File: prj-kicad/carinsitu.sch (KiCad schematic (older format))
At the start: 0 parts

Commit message: = ADD: Draw board outline, add fix holes
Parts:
- added FIX1, FIX2, FIX3, FIX4, FIX5: CONN_1, carinsitu:FIX, symbol CONN_1
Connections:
- new net GND: FIX1.1, FIX2.1, FIX3.1, FIX4.1, FIX5.1
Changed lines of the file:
@@
 EESchema Schematic File Version 2
-LIBS:power
+LIBS:cartes_v3
+LIBS:carinsitu
 LIBS:carinsitu-cache
 EELAYER 25 0
@@
 Comment4 ""
 $EndDescr
+$Comp
+L CONN_1 FIX1
+U 1 1 5D08E86D
+P 6050 6800
+F 0 "FIX1" H 6130 6800 40  0000 L CNN
+F 1 "CONN_1" H 6050 6855 30  0001 C CNN
+F 2 "carinsitu:FIX" H 6050 6800 60  0001 C CNN
+F 3 "" H 6050 6800 60  0000 C CNN
+	1    6050 6800
+	-1   0    0    1
+$EndComp
+$Comp
+L CONN_1 FIX2
+U 1 1 5D08E8D7
+P 6050 6950
+F 0 "FIX2" H 6130 6950 40  0000 L CNN
+F 1 "CONN_1" H 6050 7005 30  0001 C CNN
+F 2 "carinsitu:FIX" H 6050 6950 60  0001 C CNN
+F 3 "" H 6050 6950 60  0000 C CNN
+	1    6050 6950
+	-1   0    0    1
+$EndComp
+$Comp
+L CONN_1 FIX3
+U 1 1 5D08E908
+P 6050 7100
+F 0 "FIX3" H 6130 7100 40  0000 L CNN
+F 1 "CONN_1" H 6050 7155 30  0001 C CNN
+F 2 "carinsitu:FIX" H 6050 7100 60  0001 C CNN
+F 3 "" H 6050 7100 60  0000 C CNN
+	1    6050 7100
+	-1   0    0    1
+$EndComp
+$Comp
+L CONN_1 FIX4
+U 1 1 5D08E927
+P 6050 7250
+F 0 "FIX4" H 6130 7250 40  0000 L CNN
+F 1 "CONN_1" H 6050 7305 30  0001 C CNN
+F 2 "carinsitu:FIX" H 6050 7250 60  0001 C CNN
+F 3 "" H 6050 7250 60  0000 C CNN
+	1    6050 7250
+	-1   0    0    1
+$EndComp
+$Comp
+L CONN_1 FIX5
+U 1 1 5D08E968
+P 6050 7400
+F 0 "FIX5" H 6130 7400 40  0000 L CNN
+F 1 "CONN_1" H 6050 7455 30  0001 C CNN
+F 2 "carinsitu:FIX" H 6050 7400 60  0001 C CNN
+F 3 "" H 6050 7400 60  0000 C CNN
+	1    6050 7400
+	-1   0    0    1
+$EndComp
+$Comp
+L GND #PWR01
+U 1 1 5D08EA24
+P 6300 7500
+F 0 "#PWR01" H 6300 7500 30  0001 C CNN
+F 1 "GND" H 6300 7430 30  0001 C CNN
+F 2 "" H 6300 7500 60  0000 C CNN
+F 3 "" H 6300 7500 60  0000 C CNN
+	1    6300 7500
+	1    0    0    -1
+$EndComp
+Wire Wire Line
+	6200 6800 6300 6800
+Wire Wire Line
+	6300 6800 6300 7500
+Wire Wire Line
+	6200 6950 6300 6950
+Connection ~ 6300 6950
+Wire Wire Line
+	6200 7100 6300 7100
+Connection ~ 6300 7100
+Wire Wire Line
+	6200 7250 6300 7250
+Connection ~ 6300 7250
+Wire Wire Line
+	6200 7400 6300 7400
+Connection ~ 6300 7400
 $EndSCHEMATC

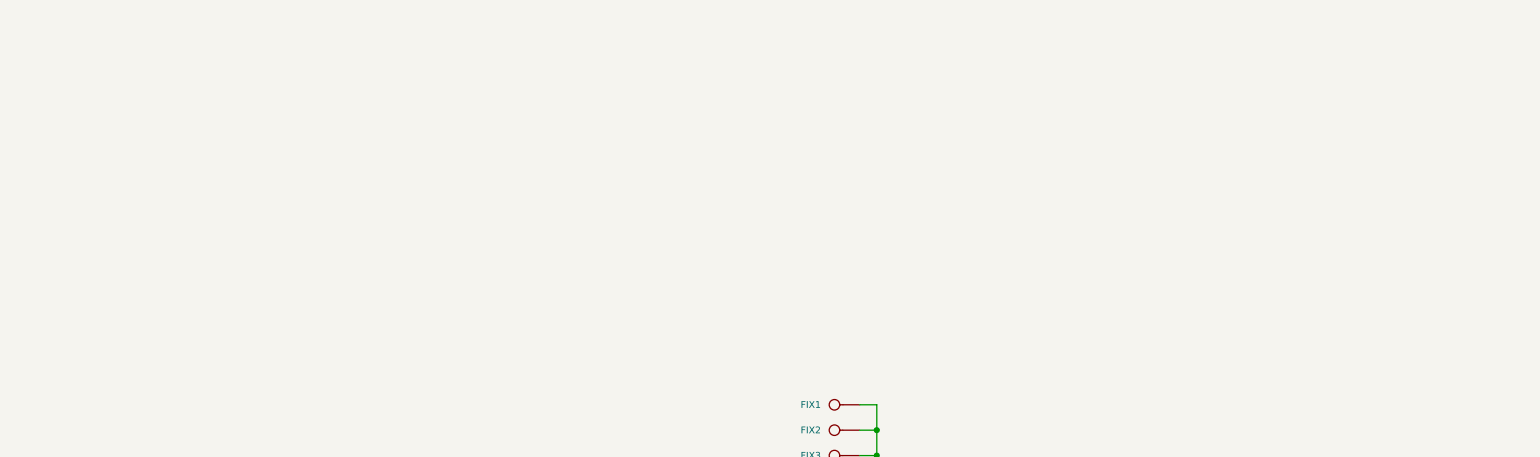
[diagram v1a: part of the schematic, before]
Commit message: = ADD: Place headlight LEDs, motor connector and ESC outline
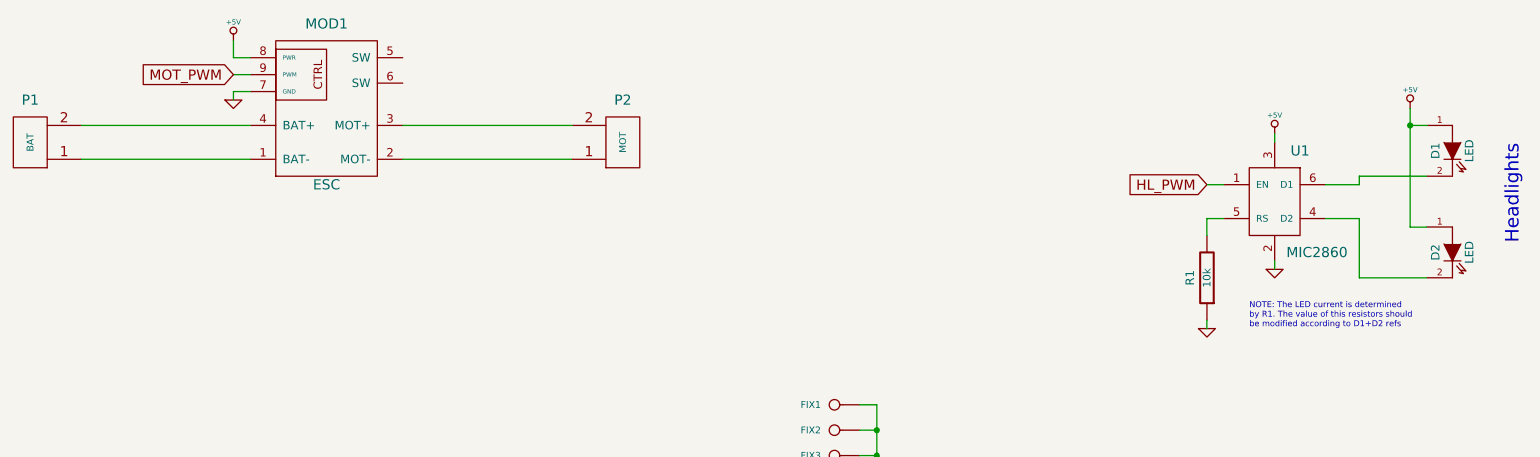
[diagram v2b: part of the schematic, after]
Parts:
- added D1, D2: LED, carinsitu:LED, symbol LED
- added MOD1: ESC, carinsitu:ESC, symbol ESC
- added P1: BAT, symbol CONN_2
- added P2: MOT, carinsitu:CONN_JST-XH-2, symbol CONN_2
- added R1: 10k, carinsitu:SMD0805, symbol R
- added U1: MIC2860, carinsitu:SOT23-6, symbol MIC2860
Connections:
- net GND: now also MOD1.7 (GND), R1.1, U1.2
- new net: MOD1.1 (BAT-), P1.1 (P1)
- new net: MOD1.4 (BAT+), P1.2 (PM)
- new net: MOD1.2 (MOT-), P2.1 (P1)
- new net: MOD1.3 (MOT+), P2.2 (PM)
- new net: D2.2 (K), U1.4 (D2)
- new net: D1.2 (K), U1.6 (D1)
- new net: R1.2, U1.5 (RS)
- new net +5V: D1.1 (A), D2.1 (A), MOD1.8 (PWR), U1.3
- new net HL_PWM: U1.1 (EN)
- new net MOT_PWM: MOD1.9 (PWM)
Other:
- note added: "Headlights"
- note added: "NOTE: The LED current is determined\nby R1. The value of this resistors should\nbe modified according to D1+D2 refs"
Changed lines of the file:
@@
 EESchema Schematic File Version 2
+LIBS:carinsitu
 LIBS:cartes_v3
-LIBS:carinsitu
 LIBS:carinsitu-cache
 EELAYER 25 0
@@
 	6200 7400 6300 7400
 Connection ~ 6300 7400
+$Comp
+L CONN_2 P1
+U 1 1 5D08EFAD
+P 1300 5250
+F 0 "P1" H 1300 5000 60  0000 C CNN
+F 1 "BAT" V 1300 5250 40  0000 C CNN
+F 2 "" H 1300 5250 60  0001 C CNN
+F 3 "" H 1300 5250 60  0000 C CNN
+	1    1300 5250
+	-1   0    0    1
+$EndComp
+$Comp
+L ESC MOD1
+U 1 1 5D08F04C
+P 3050 5050
+F 0 "MOD1" H 3050 5550 60  0000 C CNN
+F 1 "ESC" H 3050 4600 60  0000 C CNN
+F 2 "carinsitu:ESC" H 3050 4950 60  0001 C CNN
+F 3 "" H 3050 4950 60  0000 C CNN
+	1    3050 5050
+	1    0    0    -1
+$EndComp
+$Comp
+L CONN_2 P2
+U 1 1 5D08F0D6
+P 4800 5250
+F 0 "P2" H 4800 5000 60  0000 C CNN
+F 1 "MOT" V 4800 5250 40  0000 C CNN
+F 2 "carinsitu:CONN_JST-XH-2" H 4800 5250 60  0001 C CNN
+F 3 "" H 4800 5250 60  0000 C CNN
+F 4 "JST" H 4800 5250 60  0001 C CNN "Manufacturer"
+F 5 "S2B-XH-A" H 4800 5250 60  0001 C CNN "Manuf Ref"
+F 6 "Farnell" H 4800 5250 60  0001 C CNN "Distributor"
+F 7 "1516289" H 4800 5250 60  0001 C CNN "Distrib Ref"
+	1    4800 5250
+	1    0    0    1
+$EndComp
+Wire Wire Line
+	1600 5150 2600 5150
+Wire Wire Line
+	2600 5350 1600 5350
+Wire Wire Line
+	3500 5150 4500 5150
+Wire Wire Line
+	4500 5350 3500 5350
+$Comp
+L LED D2
+U 1 1 5D132E1D
+P 9700 5900
+F 0 "D2" V 9600 5900 50  0000 C CNN
+F 1 "LED" V 9800 5900 50  0000 C CNN
+F 2 "carinsitu:LED" V 9700 5900 60  0001 C CNN
+F 3 "" V 9700 5900 60  0000 C CNN
+	1    9700 5900
+	1    0    0    1
+$EndComp
+$Comp
+L LED D1
+U 1 1 5D132EA5
+P 9700 5300
+F 0 "D1" V 9600 5300 50  0000 C CNN
+F 1 "LED" V 9800 5300 50  0000 C CNN
+F 2 "carinsitu:LED" V 9700 5300 60  0001 C CNN
+F 3 "" V 9700 5300 60  0000 C CNN
+	1    9700 5300
+	1    0    0    1
+$EndComp
+$Comp
+L MIC2860 U1
+U 1 1 5D1330CD
+P 8650 5600
+F 0 "U1" H 8800 5900 60  0000 C CNN
+F 1 "MIC2860" H 8900 5300 60  0000 C CNN
+F 2 "carinsitu:SOT23-6" H 8650 5600 60  0001 C CNN
+F 3 "" H 8650 5600 60  0000 C CNN
+	1    8650 5600
+	1    0    0    -1
+$EndComp
+Wire Wire Line
+	8950 5500 9150 5500
+Wire Wire Line
+	8950 5700 9150 5700
+Wire Wire Line
+	9150 5700 9150 6050
+Wire Wire Line
+	9150 6050 9550 6050
+Wire Wire Line
+	9150 5500 9150 5450
+Wire Wire Line
+	9150 5450 9550 5450
+$Comp
+L GND #PWR02
+U 1 1 5D133417
+P 2500 5000
+F 0 "#PWR02" H 2500 5000 30  0001 C CNN
+F 1 "GND" H 2500 4930 30  0001 C CNN
+F 2 "" H 2500 5000 60  0000 C CNN
+F 3 "" H 2500 5000 60  0000 C CNN
+	1    2500 5000
+	1    0    0    -1
+$EndComp
+Wire Wire Line
+	2500 5000 2500 4950
+Wire Wire Line
+	2500 4950 2600 4950
+$Comp
+L +5V #PWR03
+U 1 1 5D133572
+P 2500 4650
+F 0 "#PWR03" H 2500 4610 30  0001 C CNN
+F 1 "+5V" H 2500 4760 30  0000 C CNN
+F 2 "" H 2500 4650 60  0000 C CNN
+F 3 "" H 2500 4650 60  0000 C CNN
+	1    2500 4650
+	1    0    0    -1
+$EndComp
+Wire Wire Line
+	2500 4650 2500 4750
+Wire Wire Line
+	2500 4750 2600 4750
+Text GLabel 2500 4850 0    60   Input ~ 0
+MOT_PWM
+Wire Wire Line
+	2500 4850 2600 4850
+$Comp
+L +5V #PWR04
+U 1 1 5D133751
+P 9450 5050
+F 0 "#PWR04" H 9450 5010 30  0001 C CNN
+F 1 "+5V" H 9450 5160 30  0000 C CNN
+F 2 "" H 9450 5050 60  0000 C CNN
+F 3 "" H 9450 5050 60  0000 C CNN
+	1    9450 5050
+	1    0    0    -1
+$EndComp
+Wire Wire Line
+	9450 5050 9450 5750
+Wire Wire Line
+	9450 5150 9550 5150
+Wire Wire Line
+	9450 5750 9550 5750
+Connection ~ 9450 5150
+Text Notes 10100 5850 1    80   ~ 0
+Headlights
+$Comp
+L +5V #PWR05
+U 1 1 5D133888
+P 8650 5200
+F 0 "#PWR05" H 8650 5160 30  0001 C CNN
+F 1 "+5V" H 8650 5310 30  0000 C CNN
+F 2 "" H 8650 5200 60  0000 C CNN
+F 3 "" H 8650 5200 60  0000 C CNN
+	1    8650 5200
+	1    0    0    -1
+$EndComp
+Wire Wire Line
+	8650 5200 8650 5250
+Wire Wire Line
+	8650 6000 8650 5950
+$Comp
+L GND #PWR06
+U 1 1 5D133907
+P 8650 6000
+F 0 "#PWR06" H 8650 6000 30  0001 C CNN
+F 1 "GND" H 8650 5930 30  0001 C CNN
+F 2 "" H 8650 6000 60  0000 C CNN
+F 3 "" H 8650 6000 60  0000 C CNN
+	1    8650 6000
+	1    0    0    -1
+$EndComp
+Text GLabel 8250 5500 0    60   Input ~ 0
+HL_PWM
+Wire Wire Line
+	8250 5500 8350 5500
+$Comp
+L R R1
+U 1 1 5D133B4E
+P 8250 6050
+F 0 "R1" V 8350 6050 50  0000 C CNN
+F 1 "10k" V 8250 6050 45  0000 C CNN
+F 2 "carinsitu:SMD0805" H 8250 6050 60  0001 C CNN
+F 3 "" H 8250 6050 60  0000 C CNN
+	1    8250 6050
+	-1   0    0    1
+$EndComp
+$Comp
+L GND #PWR07
+U 1 1 5D133C2F
+P 8250 6350
+F 0 "#PWR07" H 8250 6350 30  0001 C CNN
+F 1 "GND" H 8250 6280 30  0001 C CNN
+F 2 "" H 8250 6350 60  0000 C CNN
+F 3 "" H 8250 6350 60  0000 C CNN
+	1    8250 6350
+	1    0    0    -1
+$EndComp
+Wire Wire Line
+	8250 6350 8250 6300
+Wire Wire Line
+	8250 5800 8250 5700
+Wire Wire Line
+	8250 5700 8350 5700
+Text Notes 8500 6350 0    35   ~ 0
+NOTE: The LED current is determined\nby R1. The value of this resistors should\nbe modified according to D1+D2 refs
 $EndSCHEMATC

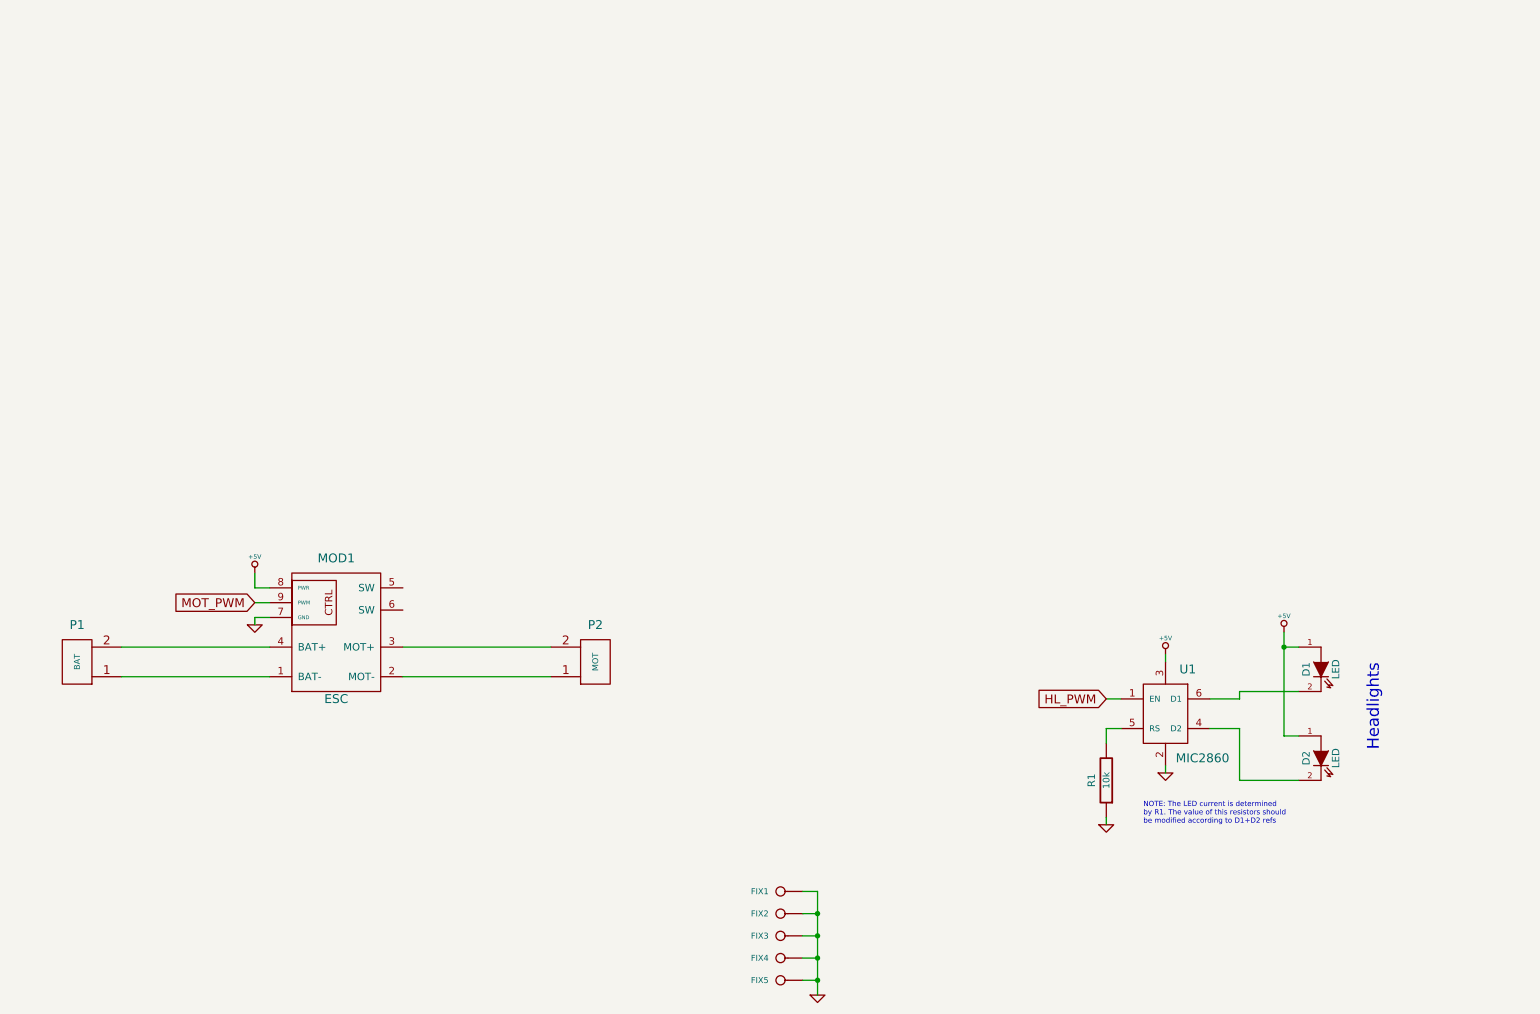
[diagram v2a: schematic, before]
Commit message: = ADD: Create ESP32 interface ; create schematics and footprint for Wemos D1-Mini (not fully routed)
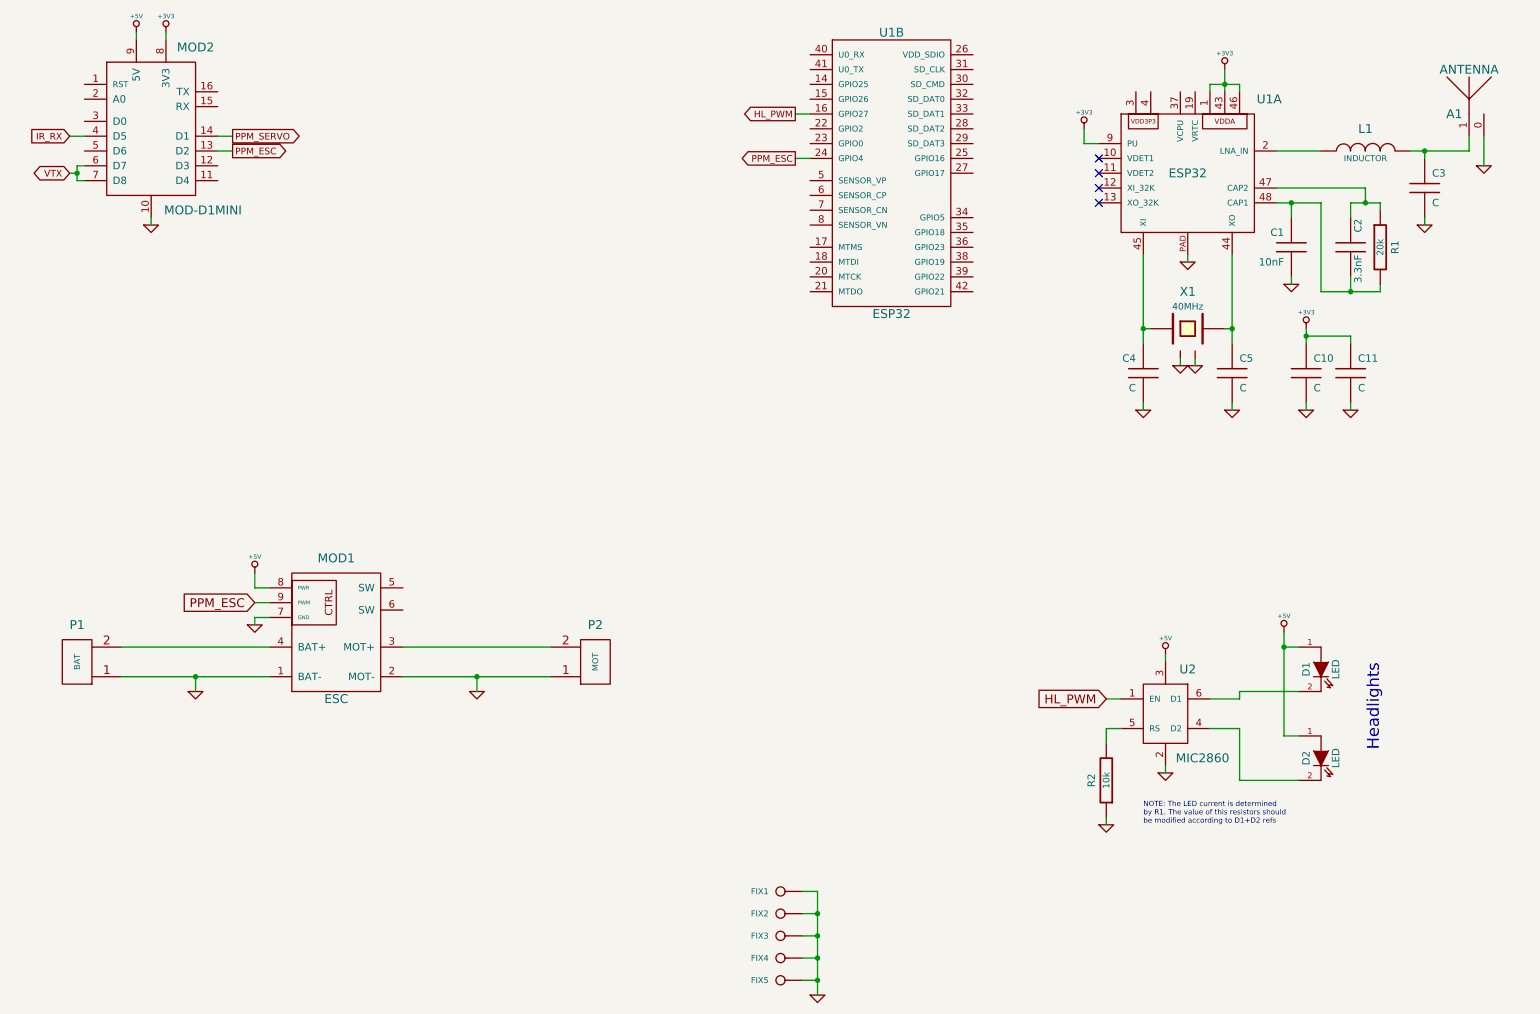
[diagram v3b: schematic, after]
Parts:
- added A1: ANTENNA, carinsitu:CONN_UFL-R-SMT-1, symbol ANTENNA
- added C1: 10nF, carinsitu:SMD0603, symbol C
- added C10, C11, C3, C4, C5: C, carinsitu:SMD0603, symbol C
- added C2: 3.3nF, carinsitu:SMD0603, symbol C
- added L1: INDUCTOR, carinsitu:SMD0603, symbol INDUCTOR
- added MOD2: MOD-D1MINI, symbol MOD-D1MINI
- added R1: 20k, carinsitu:SMD0603, symbol R
- added U1: ESP32, carinsitu:QFN48-04, symbol ESP32
- added X1: 40MHz, carinsitu:Q_3.2x2.5, symbol CRYSTAL4
- P1: footprint (none) -> carinsitu:CONN_61300211021; Distrib Ref (none) -> 2356176; Distributor (none) -> Farnell; Manuf Ref (none) -> 61300211021; Manufacturer (none) -> Wurth
- renumbered R1 to R2, U1 to U2
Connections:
- net +5V: now also MOD2.9 (5V)
- net GND: now also MOD1.1 (BAT-), MOD1.2 (MOT-), P1.1 (P1), P2.1 (P1), A1.0, C1.2, C10.2, C11.2, C3.2, C4.2, C5.2, MOD2.10, U1.PAD, X1.2, X1.4
- net HL_PWM: now also U1.16 (GPIO27)
- net MOT_PWM renamed PPM_ESC
- net PPM_ESC: now also MOD2.13 (D2), U1.24 (GPIO4)
- new net: L1.1, U1.2 (LNA_IN)
- new net: C5.1, U1.44 (XO), X1.1
- new net: C4.1, U1.45 (XI), X1.3
- new net: C2.1, R1.1, U1.47 (CAP2)
- new net: C1.1, C2.2, R1.2, U1.48 (CAP1)
- new net: A1.1, C3.1, L1.2
- new net +3V3: C10.1, C11.1, MOD2.8 (3V3), U1.1, U1.43, U1.46, U1.9 (PU)
- new net IR_RX: MOD2.4 (D5)
- new net PPM_SERVO: MOD2.14 (D1)
- new net VTX: MOD2.6 (D7), MOD2.7 (D8)
- no-connect marks 0 -> 4
